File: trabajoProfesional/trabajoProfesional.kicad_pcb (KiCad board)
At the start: 2 copper layers, 20.6 x 17.1 mm, 47 parts, among them T1 MPMOS, U1 1501

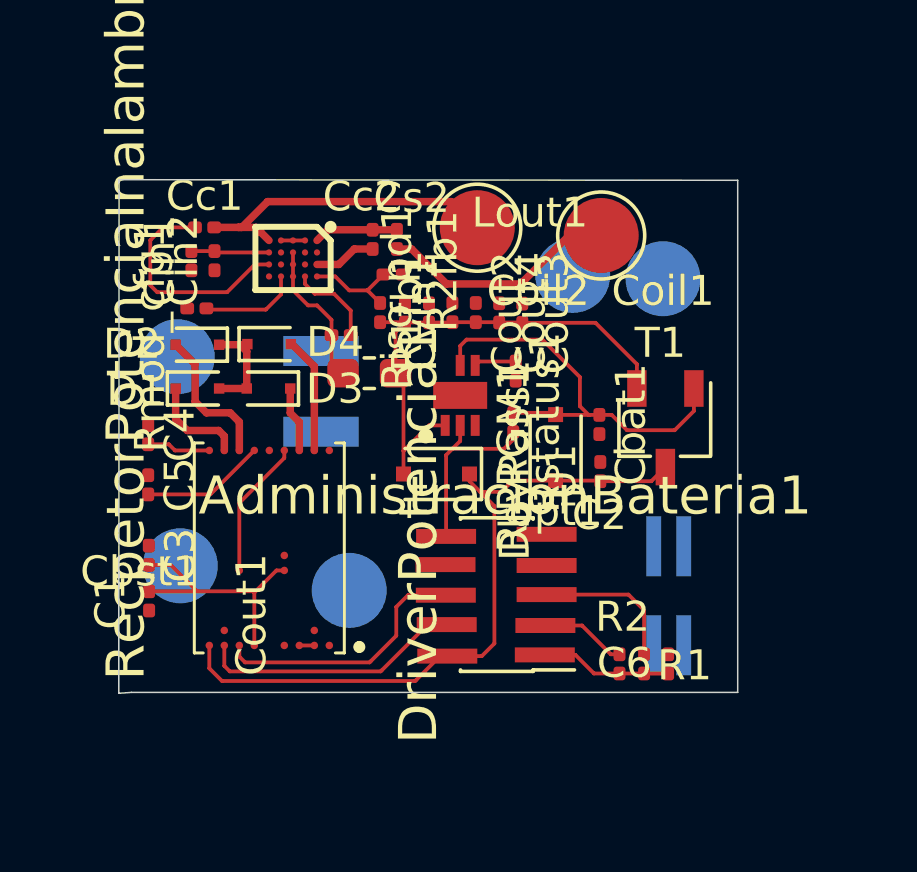
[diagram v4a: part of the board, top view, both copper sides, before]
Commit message: doble capa incluyendo el modelo 3D
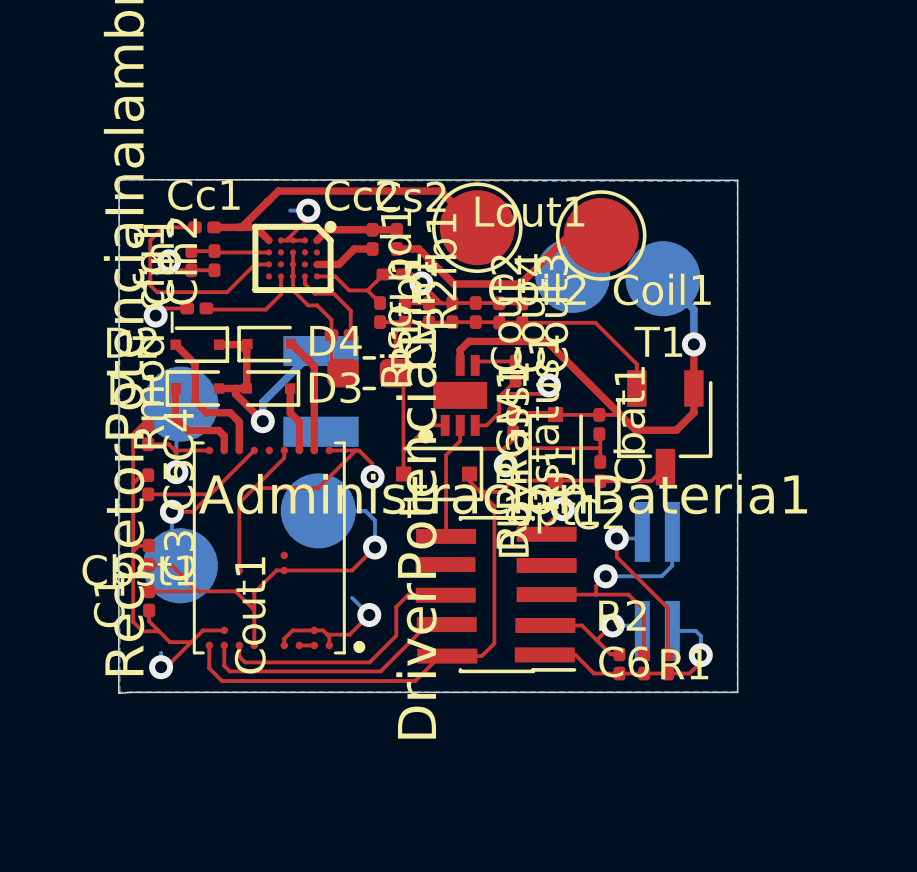
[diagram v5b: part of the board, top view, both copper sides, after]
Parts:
- moved 10V1 2.84 mm to (66.3, 72.1)
- moved HV-1 1.58 mm to (61.7, 68.5)
- moved SensorPresion1 0.61 mm to (77.6, 74.4), turned to 90 degrees
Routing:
- net GND: track 5.42 -> 52.4 mm, vias 0 -> 10
- net 10V: track 8.57 -> 15.1 mm, vias 0 -> 1
- net Net-(C6-Pad1): track 0.00 -> 5.51 mm, vias 0 -> 1
- net Net-(D1-Pad2): track 3.42 -> 8.17 mm, vias 0 -> 1
- net +Bat: track 13.9 -> 18.3 mm, vias 0 -> 1
- net SDAPresion: track 4.94 -> 9.17 mm, vias 0 -> 1
- net +HV: track 4.14 -> 7.58 mm, vias 0 -> 1
- net Net-(C6-Pad2): track 4.37 -> 7.51 mm, vias 0 -> 1
- net -HV: track 2.12 -> 5.20 mm, vias 0 -> 1
- net SCLPresion: track 2.87 -> 4.68 mm, vias 0 -> 1
- added copper zone on B.Cu, net GND
